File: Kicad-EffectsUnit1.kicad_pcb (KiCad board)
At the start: 2 copper layers, 100 x 100 mm, 0 parts

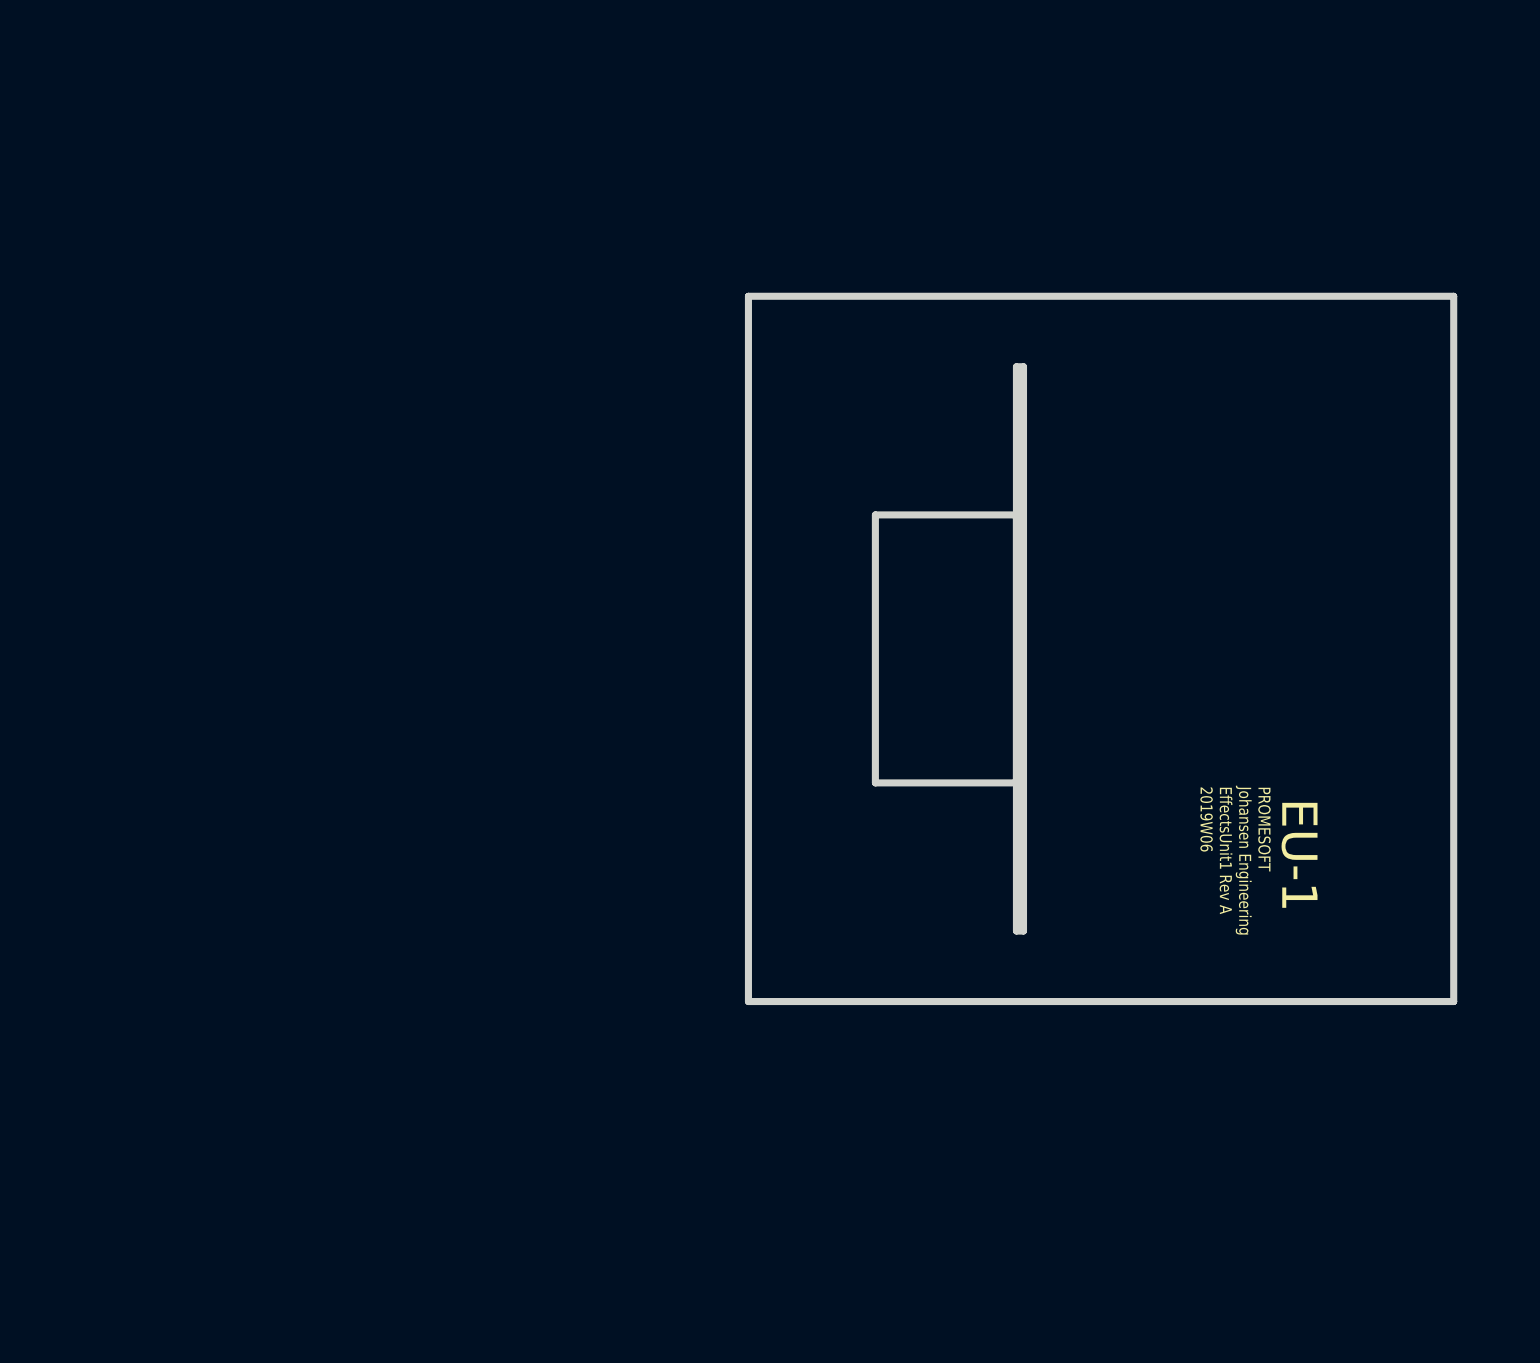
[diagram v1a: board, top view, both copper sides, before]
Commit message: anti latchup initiated
inspiration:
https://www.electrosmash.com/images/tech/pt2399/PT2399_Transistor_Current_Sink_Pin6.png
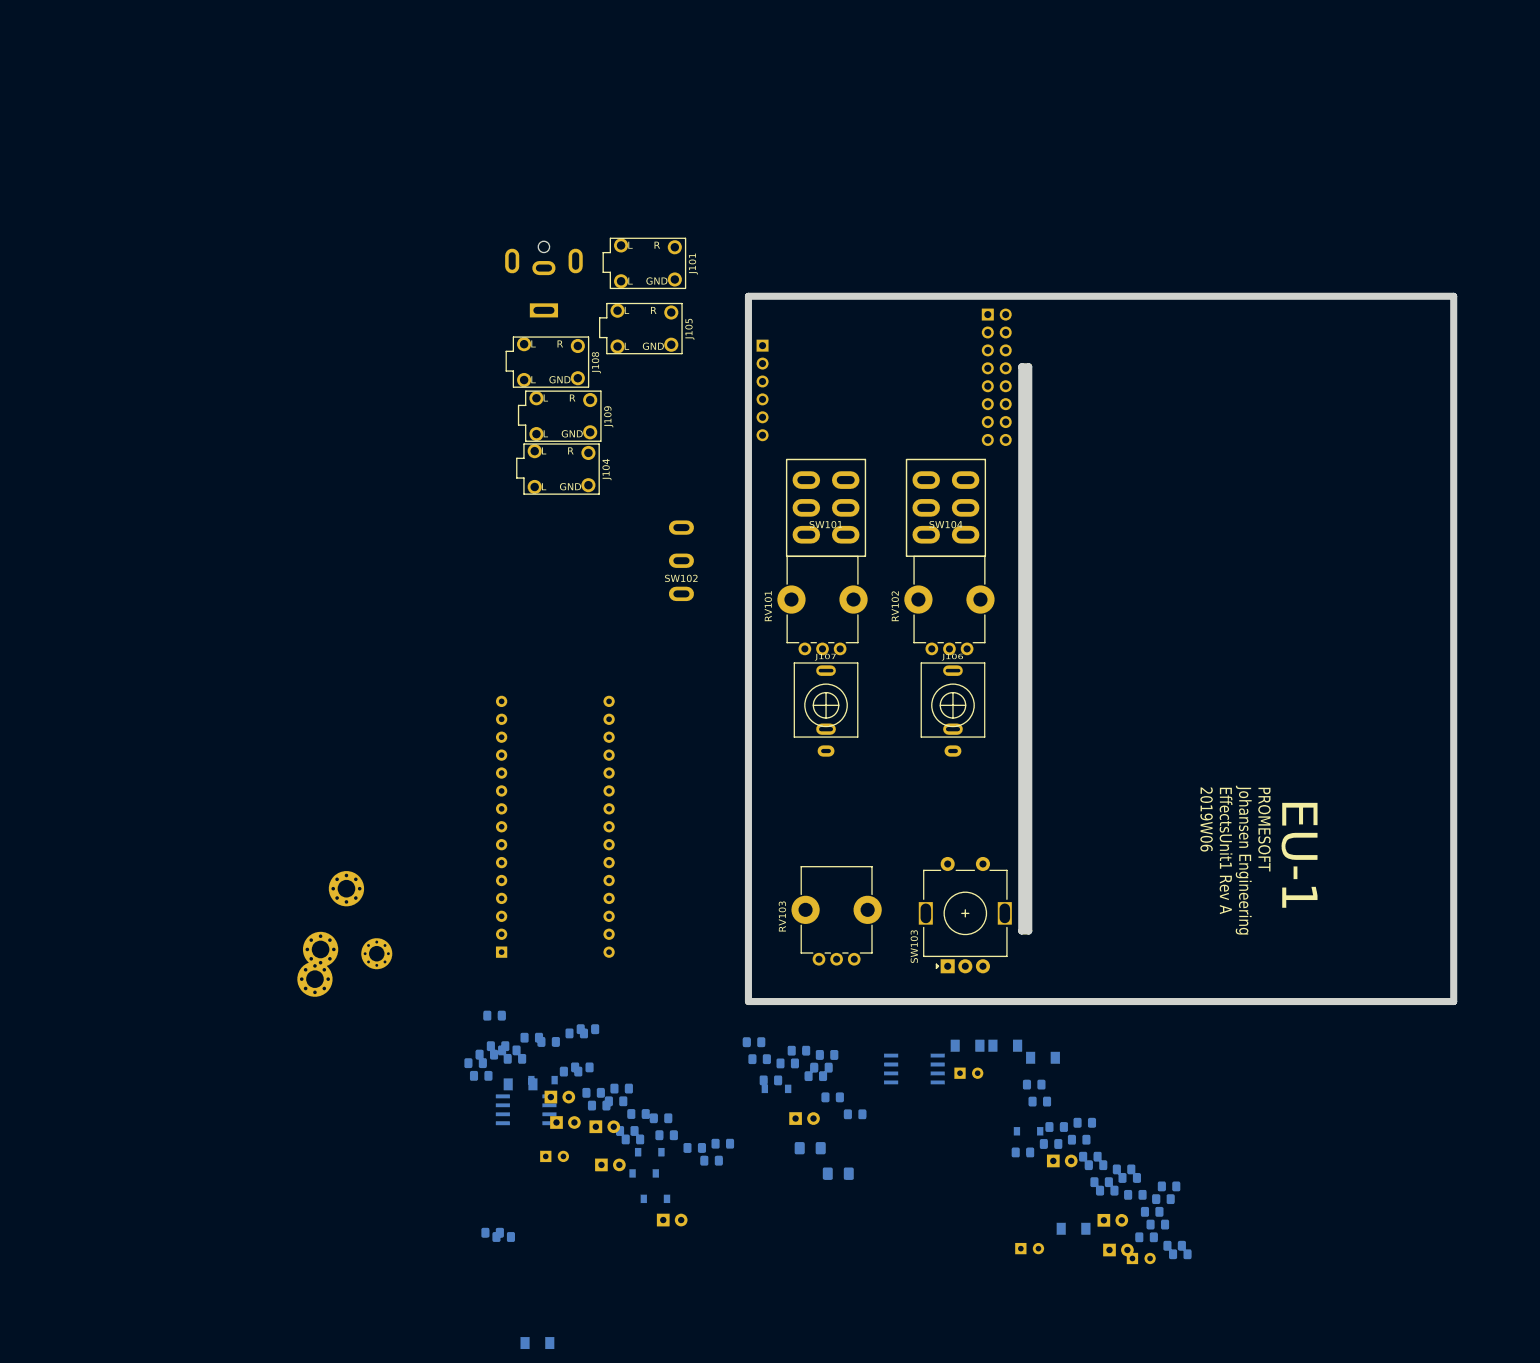
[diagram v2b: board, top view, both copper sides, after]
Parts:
- added A101: Arduino_Nano_v3.x, Module:Arduino_Nano, B.Cu at (65.0, 143.0)
- added C101: 100uF, Capacitor_THT:CP_Radial_D5.0mm_P2.50mm, B.Cu at (138.6, 185.0)
- added C102: 100n, Capacitor_SMD:C_0805_2012Metric_Pad1.15x1.40mm_HandSolder, B.Cu at (161.2, 185.8)
- added C103: 100n, Capacitor_SMD:C_0805_2012Metric_Pad1.15x1.40mm_HandSolder, B.Cu at (66.1, 156.9)
- added C104: 100n, Capacitor_SMD:C_0805_2012Metric_Pad1.15x1.40mm_HandSolder, B.Cu at (64.0, 152.0)
- added C105: 100uF, Capacitor_THT:CP_Radial_D5.0mm_P2.50mm, B.Cu at (130.0, 160.2)
- added C106: 100uF 16v, Capacitor_THT:CP_Radial_D5.0mm_P2.50mm, B.Cu at (71.3, 172.0)
- added C107: 100n, Capacitor_SMD:C_0805_2012Metric_Pad1.15x1.40mm_HandSolder, B.Cu at (64.5, 156.3)
- added C108: 100n, Capacitor_SMD:C_0805_2012Metric_Pad1.15x1.40mm_HandSolder, B.Cu at (62.9, 157.5)
- added C109: 100n, Capacitor_SMD:C_0805_2012Metric_Pad1.15x1.40mm_HandSolder, B.Cu at (65.3, 183.4)
- added C110: 100uF 16v, Capacitor_THT:CP_Radial_D5.0mm_P2.50mm, B.Cu at (154.4, 186.4)
- added C111: 100n, Capacitor_SMD:C_0805_2012Metric_Pad1.15x1.40mm_HandSolder, B.Cu at (62.1, 160.5)
- added C112: 100n, Capacitor_SMD:C_0805_2012Metric_Pad1.15x1.40mm_HandSolder, B.Cu at (61.3, 158.7)
- added C113: 100n, Capacitor_SMD:C_0805_2012Metric_Pad1.15x1.40mm_HandSolder, B.Cu at (148.5, 172.0)
- added C114: 47n, Capacitor_SMD:C_0805_2012Metric_Pad1.15x1.40mm_HandSolder, B.Cu at (138.9, 171.4)
- added C115: 100n, Capacitor_SMD:C_0805_2012Metric_Pad1.15x1.40mm_HandSolder, B.Cu at (69.3, 155.1)
- added C116: 100n, Capacitor_SMD:C_0805_2012Metric_Pad1.15x1.40mm_HandSolder, B.Cu at (150.9, 176.8)
- added C117: 33n, Capacitor_SMD:C_0805_2012Metric_Pad1.15x1.40mm_HandSolder, B.Cu at (160.4, 184.6)
- added C118: 100n, Capacitor_SMD:C_0805_2012Metric_Pad1.15x1.40mm_HandSolder, B.Cu at (94.8, 172.6)
- added C119: 33n, Capacitor_SMD:C_0805_2012Metric_Pad1.15x1.40mm_HandSolder, B.Cu at (154.1, 175.0)
- added C120: 44n, Capacitor_SMD:C_0805_2012Metric_Pad1.15x1.40mm_HandSolder, B.Cu at (107.2, 157.0)
- added C121: 44n, Capacitor_SMD:C_0805_2012Metric_Pad1.15x1.40mm_HandSolder, B.Cu at (84.4, 166.0)
- added D101: 1N1007, Diode_SMD:D_SOD-123, B.Cu at (70.9, 161.1)
- added D102: 1N1007, Diode_SMD:D_SOD-123, B.Cu at (85.2, 174.4)
- added D103: LED1, LED_THT:LED_D3.0mm, B.Cu at (72.8, 167.2)
- added D104: LED2, LED_THT:LED_D3.0mm, B.Cu at (79.2, 173.2)
- added D105: LED3, LED_THT:LED_D3.0mm, B.Cu at (151.2, 185.2)
- added D106: 1N1007, Diode_SMD:D_SOD-123, B.Cu at (139.7, 168.4)
- added D107: LED4, LED_THT:LED_D3.0mm, B.Cu at (87.9, 181.0)
- added D108: 1N1007, Diode_SMD:D_SOD-123, B.Cu at (86.8, 178.0)
- added D109: LED_Out10, LED_THT:LED_D3.0mm, B.Cu at (72.0, 163.5)
- added D110: 1N1007, Diode_SMD:D_SOD-123, B.Cu at (86.0, 171.4)
- added D111: 1N1007, Diode_SMD:D_SOD-123, B.Cu at (104.0, 162.4)
- added D112: LED_Out11, LED_THT:LED_D3.0mm, B.Cu at (78.4, 167.8)
- added D113: LED_Out12, LED_THT:LED_D3.0mm, B.Cu at (143.2, 172.6)
- added D114: LED_Out13, LED_THT:LED_D3.0mm, B.Cu at (150.4, 181.0)
- added D115: LL4148, Diode_SMD:D_MiniMELF, B.Cu at (146.1, 182.2)
- added D116: LL4148, Diode_SMD:D_MiniMELF, B.Cu at (67.7, 161.7)
- added D117: LED_Out11, LED_SMD:LED_0805_2012Metric_Pad1.15x1.40mm_HandSolder, B.Cu at (63.7, 182.8)
- added D118: LED_CV2, LED_THT:LED_D3.0mm, B.Cu at (106.7, 166.6)
- added D119: LL4148, Diode_SMD:D_MiniMELF, B.Cu at (141.8, 158.0)
- added D120: LL4148, Diode_SMD:D_MiniMELF, B.Cu at (136.4, 156.3)
- added D121: LL4148, Diode_SMD:D_MiniMELF, B.Cu at (131.1, 156.3)
- added D122: LL4148, Diode_SMD:D_MiniMELF, B.Cu at (70.1, 198.4)
- added F101: Polyfuse, Fuse:Fuse_1206_3216Metric_Pad1.42x1.75mm_HandSolder, B.Cu at (108.8, 170.8)
- added F102: Polyfuse, Fuse:Fuse_1206_3216Metric_Pad1.42x1.75mm_HandSolder, B.Cu at (112.7, 174.4)
- added H101: 2,5mm, MountingHole:MountingHole_2.5mm_Pad_Via, B.Cu at (39.3, 142.6)
- added H102: 2,5mm, MountingHole:MountingHole_2.5mm_Pad_Via, B.Cu at (38.5, 146.8)
- added H103: 2,2mm, MountingHole:MountingHole_2.5mm_Pad_Via, B.Cu at (43.0, 134.0)
- added H104: 2,2mm, MountingHole:MountingHole_2.2mm_M2_Pad_Via, B.Cu at (47.3, 143.2)
- added J101: In7, Connector_Audio:AudioJack3StereoNarrow-PJ-321, F.Cu at (85.8, 45.3)
- added J102: Doepfer connector, Connector_PinSocket_2.54mm:PinSocket_2x08_P2.54mm_Vertical, B.Cu at (133.9, 52.6)
- added J103: Vin 7-12v, Connector_BarrelJack:BarrelJack_CUI_PJ-063AH_Horizontal, B.Cu at (71.0, 52.0)
- added J104: In6, Connector_Audio:AudioJack3StereoNarrow-PJ-321, F.Cu at (73.5, 74.5)
- added J105: In3, Connector_Audio:AudioJack3StereoNarrow-PJ-321, F.Cu at (85.2, 54.6)
- added J106: Out10, AJ-Dropbox-Kicad:PJ301SM, F.Cu at (129.0, 108.0)
- added J107: Out11, AJ-Dropbox-Kicad:PJ301SM, F.Cu at (111.0, 108.0)
- added J108: Out12, Connector_Audio:AudioJack3StereoNarrow-PJ-321, F.Cu at (72.0, 59.3)
- added J109: Out13, Connector_Audio:AudioJack3StereoNarrow-PJ-321, F.Cu at (73.8, 67.0)
- added J110: Power Conn, Connector_PinHeader_2.54mm:PinHeader_1x06_P2.54mm_Vertical, B.Cu at (102.0, 57.0)
- added R101: 10k, Resistor_SMD:R_0805_2012Metric_Pad1.15x1.40mm_HandSolder, B.Cu at (142.9, 170.2)
- added R102: 10M, Resistor_SMD:R_0805_2012Metric_Pad1.15x1.40mm_HandSolder, B.Cu at (158.0, 181.6)
- added R103: 10k, Resistor_SMD:R_0805_2012Metric_Pad1.15x1.40mm_HandSolder, B.Cu at (150.1, 175.6)
- added R104: 10k, Resistor_SMD:R_0805_2012Metric_Pad1.15x1.40mm_HandSolder, B.Cu at (71.7, 155.7)
- added R105: 10k, Resistor_SMD:R_0805_2012Metric_Pad1.15x1.40mm_HandSolder, B.Cu at (83.6, 169.6)
- added R106: 680R, Resistor_SMD:R_0805_2012Metric_Pad1.15x1.40mm_HandSolder, B.Cu at (115.1, 166.0)
- added R107: 10k, Resistor_SMD:R_0805_2012Metric_Pad1.15x1.40mm_HandSolder, B.Cu at (103.2, 161.2)
- added R108: 10k, Resistor_SMD:R_0805_2012Metric_Pad1.15x1.40mm_HandSolder, B.Cu at (101.6, 158.2)
- added R109: 680R, Resistor_SMD:R_0805_2012Metric_Pad1.15x1.40mm_HandSolder, B.Cu at (141.3, 164.2)
- added R110: 680R, Resistor_SMD:R_0805_2012Metric_Pad1.15x1.40mm_HandSolder, B.Cu at (111.9, 163.6)
- added R111: 11k, Resistor_SMD:R_0805_2012Metric_Pad1.15x1.40mm_HandSolder, B.Cu at (100.8, 155.8)
- added R112: 11k, Resistor_SMD:R_0805_2012Metric_Pad1.15x1.40mm_HandSolder, B.Cu at (156.5, 183.4)
- added R113: 680R, Resistor_SMD:R_0805_2012Metric_Pad1.15x1.40mm_HandSolder, B.Cu at (78.0, 162.9)
- added R114: 680R, Resistor_SMD:R_0805_2012Metric_Pad1.15x1.40mm_HandSolder, B.Cu at (82.8, 168.4)
- added R115: 110R, Resistor_SMD:R_0805_2012Metric_Pad1.15x1.40mm_HandSolder, B.Cu at (149.3, 173.2)
- added R116: 680R, Resistor_SMD:R_0805_2012Metric_Pad1.15x1.40mm_HandSolder, B.Cu at (157.2, 179.8)
- added R117: 11k, Resistor_SMD:R_0805_2012Metric_Pad1.15x1.40mm_HandSolder, B.Cu at (154.9, 177.4)
- added R118: 680R, Resistor_SMD:R_0805_2012Metric_Pad1.15x1.40mm_HandSolder, B.Cu at (143.7, 167.8)
- added R119: 22k, Resistor_SMD:R_0805_2012Metric_Pad1.15x1.40mm_HandSolder, B.Cu at (92.4, 170.8)
- added R120: 22k, Resistor_SMD:R_0805_2012Metric_Pad1.15x1.40mm_HandSolder, B.Cu at (105.6, 158.8)
- added R121: 680R, Resistor_SMD:R_0805_2012Metric_Pad1.15x1.40mm_HandSolder, B.Cu at (109.6, 160.6)
- added R122: 220R, Resistor_SMD:R_0805_2012Metric_Pad1.15x1.40mm_HandSolder, B.Cu at (74.9, 159.9)
- added R123: 220R, Resistor_SMD:R_0805_2012Metric_Pad1.15x1.40mm_HandSolder, B.Cu at (78.8, 164.7)
- added R124: 220k, Resistor_SMD:R_0805_2012Metric_Pad1.15x1.40mm_HandSolder, B.Cu at (66.9, 158.1)
- added R125: 10k, Resistor_SMD:R_0805_2012Metric_Pad1.15x1.40mm_HandSolder, B.Cu at (76.4, 159.3)
- added R126: 10k, Resistor_SMD:R_0805_2012Metric_Pad1.15x1.40mm_HandSolder, B.Cu at (88.4, 169.0)
- added R127: 10k, Resistor_SMD:R_0805_2012Metric_Pad1.15x1.40mm_HandSolder, B.Cu at (81.2, 164.1)
- added R128: 3k3, Resistor_SMD:R_0805_2012Metric_Pad1.15x1.40mm_HandSolder, B.Cu at (87.6, 166.6)
- added R129: 33k, Resistor_SMD:R_0805_2012Metric_Pad1.15x1.40mm_HandSolder, B.Cu at (146.9, 169.6)
- added R130: 133R, Resistor_SMD:R_0805_2012Metric_Pad1.15x1.40mm_HandSolder, B.Cu at (75.7, 154.5)
- added R131: 33k, Resistor_SMD:R_0805_2012Metric_Pad1.15x1.40mm_HandSolder, B.Cu at (153.3, 173.8)
- added R132: 33k, Resistor_SMD:R_0805_2012Metric_Pad1.15x1.40mm_HandSolder, B.Cu at (110.3, 159.4)
- added R133: 330k, Resistor_SMD:R_0805_2012Metric_Pad1.15x1.40mm_HandSolder, B.Cu at (158.8, 178.0)
- added R134: 33k, Resistor_SMD:R_0805_2012Metric_Pad1.15x1.40mm_HandSolder, B.Cu at (82.0, 162.3)
- added R135: 44k, Resistor_SMD:R_0805_2012Metric_Pad1.15x1.40mm_HandSolder, B.Cu at (140.5, 161.8)
- added R136: 44k, Resistor_SMD:R_0805_2012Metric_Pad1.15x1.40mm_HandSolder, B.Cu at (147.7, 167.2)
- added R137: 144R, Resistor_SMD:R_0805_2012Metric_Pad1.15x1.40mm_HandSolder, B.Cu at (77.2, 153.9)
- added R138: 44k, Resistor_SMD:R_0805_2012Metric_Pad1.15x1.40mm_HandSolder, B.Cu at (159.6, 176.2)
- added R139: 44k, Resistor_SMD:R_0805_2012Metric_Pad1.15x1.40mm_HandSolder, B.Cu at (111.1, 157.6)
- added R140: 440k, Resistor_SMD:R_0805_2012Metric_Pad1.15x1.40mm_HandSolder, B.Cu at (96.4, 170.2)
- added RV101: 10k, Potentiometer_THT:Potentiometer_Alps_RK09K_Single_Vertical, F.Cu at (113.0, 100.0)
- added RV102: 10k, Potentiometer_THT:Potentiometer_Alps_RK09K_Single_Vertical, F.Cu at (131.0, 100.0)
- added RV103: 100k, Potentiometer_THT:Potentiometer_Alps_RK09K_Single_Vertical, F.Cu at (115.0, 144.0)
- added SW101: SW_DPDT_x2, AJ-Dropbox-Kicad:SPDTx2, F.Cu at (111.0, 80.0)
- added SW102: SW_SPDT, AJ-Dropbox-Kicad:SP1MS1, F.Cu at (90.5, 87.5)
- added SW103: Rotary_Encoder_Switch, Rotary_Encoder:RotaryEncoder_Alps_EC11E-Switch_Vertical_H20mm, F.Cu at (128.2, 145.0)
- added SW104: SW_DPDT_x2, AJ-Dropbox-Kicad:SPDTx2, F.Cu at (128.0, 80.0)
- added U101: TL072, AJ-Dropbox-Kicad:AJ_SO-8_5.3x6.2mm_P1.27mm, B.Cu at (123.5, 159.6)
- added U102: TL072, AJ-Dropbox-Kicad:AJ_SO-8_5.3x6.2mm_P1.27mm, B.Cu at (68.5, 165.3)
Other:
- outline, holes or cut-outs redrawn

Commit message: Footprints
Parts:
- added C201: 100uF 16v, Capacitor_THT:CP_Radial_D5.0mm_P2.50mm, F.Cu at (154.6, 35.7)
- added C202: 100n, Capacitor_SMD:C_0805_2012Metric_Pad1.15x1.40mm_HandSolder, F.Cu at (204.3, 24.4)
- added C203: 100n, Capacitor_SMD:C_0805_2012Metric_Pad1.15x1.40mm_HandSolder, F.Cu at (204.3, 26.3)
- added C204: 100n, Capacitor_SMD:C_0805_2012Metric_Pad1.15x1.40mm_HandSolder, F.Cu at (193.1, 26.3)
- added C205: 100uF 16v, Capacitor_THT:CP_Radial_D5.0mm_P2.50mm, F.Cu at (173.1, 41.5)
- added C206: 100uF 16v, Capacitor_THT:CP_Radial_D5.0mm_P2.50mm, F.Cu at (167.5, 41.5)
- added C207: 100n, Capacitor_SMD:C_0805_2012Metric_Pad1.15x1.40mm_HandSolder, F.Cu at (195.8, 36.1)
- added C208: 100n, Capacitor_SMD:C_0805_2012Metric_Pad1.15x1.40mm_HandSolder, F.Cu at (188.3, 31.0)
- added C209: 100n, Capacitor_SMD:C_0805_2012Metric_Pad1.15x1.40mm_HandSolder, F.Cu at (204.2, 18.5)
- added C210: 100uF 16v, Capacitor_THT:CP_Radial_D5.0mm_P2.50mm, F.Cu at (204.0, 14.8)
- added C211: 3n3, Capacitor_SMD:C_0805_2012Metric_Pad1.15x1.40mm_HandSolder, F.Cu at (160.5, 33.9)
- added C212: 4u7, Capacitor_SMD:C_0805_2012Metric_Pad1.15x1.40mm_HandSolder, F.Cu at (160.5, 35.8)
- added C213: 4u7, Capacitor_SMD:C_0805_2012Metric_Pad1.15x1.40mm_HandSolder, F.Cu at (200.2, 19.7)
- added C214: 560p, Capacitor_SMD:C_0805_2012Metric_Pad1.15x1.40mm_HandSolder, F.Cu at (200.2, 21.7)
- added C215: 100uF 16v, Capacitor_THT:CP_Radial_D5.0mm_P2.50mm, F.Cu at (194.3, 21.5)
- added C216: 10u, Capacitor_SMD:C_0805_2012Metric_Pad1.15x1.40mm_HandSolder, F.Cu at (188.3, 33.0)
- added C217: 10u, Capacitor_SMD:C_0805_2012Metric_Pad1.15x1.40mm_HandSolder, F.Cu at (193.1, 28.3)
- added C218: 10n, Capacitor_SMD:C_0805_2012Metric_Pad1.15x1.40mm_HandSolder, F.Cu at (193.1, 30.2)
- added C219: 560p, Capacitor_SMD:C_0805_2012Metric_Pad1.15x1.40mm_HandSolder, F.Cu at (188.3, 34.9)
- added C220: 82n, Capacitor_SMD:C_0805_2012Metric_Pad1.15x1.40mm_HandSolder, F.Cu at (200.2, 23.6)
- added C221: 3n3, Capacitor_SMD:C_0805_2012Metric_Pad1.15x1.40mm_HandSolder, F.Cu at (196.8, 25.6)
- added C222: 1u, Capacitor_SMD:C_0805_2012Metric_Pad1.15x1.40mm_HandSolder, F.Cu at (184.5, 40.1)
- added C223: 100n, Capacitor_SMD:C_0805_2012Metric_Pad1.15x1.40mm_HandSolder, F.Cu at (196.8, 27.5)
- added C224: 82n, Capacitor_SMD:C_0805_2012Metric_Pad1.15x1.40mm_HandSolder, F.Cu at (203.9, 20.5)
- added C225: 100n, Capacitor_SMD:C_0805_2012Metric_Pad1.15x1.40mm_HandSolder, F.Cu at (208.0, 18.5)
- added C226: 100n, Capacitor_SMD:C_0805_2012Metric_Pad1.15x1.40mm_HandSolder, F.Cu at (203.9, 22.4)
- added D201: 1N1007, Diode_SMD:D_SOD-123, F.Cu at (188.8, 28.9)
- added D202: 1N1007, Diode_SMD:D_SOD-123, F.Cu at (155.4, 43.1)
- added D203: 1N1007, Diode_SMD:D_SOD-123, F.Cu at (188.8, 26.5)
- added D204: 5v6, Diode_SMD:D_MELF-RM10_Universal_Handsoldering, F.Cu at (159.4, 40.3)
- added D205: 1N1007, Diode_SMD:D_SOD-123, F.Cu at (160.1, 43.1)
- added J201: In, AJ-Dropbox-Kicad:PJ301SM, F.Cu at (188.1, 18.1)
- added J202: Out, AJ-Dropbox-Kicad:PJ301SM, F.Cu at (181.9, 31.9)
- added P201: HEADER_2x5_Doepfer, Connector_PinHeader_2.54mm:PinHeader_2x05_P2.54mm_Vertical, F.Cu at (179.1, 13.8)
- added Q201: BC337, Package_TO_SOT_THT:TO-92_Inline, F.Cu at (178.6, 41.9)
- added Q202: PZT2222A, Package_TO_SOT_SMD:SOT-23, F.Cu at (204.2, 29.1)
- added Q203: PZT2222A, Package_TO_SOT_SMD:SOT-23, F.Cu at (199.4, 32.2)
- added R201: 10k, Resistor_SMD:R_0805_2012Metric_Pad1.15x1.40mm_HandSolder, F.Cu at (200.6, 25.6)
- added R202: 0R, Resistor_SMD:R_0805_2012Metric_Pad1.15x1.40mm_HandSolder, F.Cu at (188.3, 36.9)
- added R203: 15k, Resistor_SMD:R_0805_2012Metric_Pad1.15x1.40mm_HandSolder, F.Cu at (192.1, 32.2)
- added R204: 0R, Resistor_SMD:R_0805_2012Metric_Pad1.15x1.40mm_HandSolder, F.Cu at (192.1, 34.1)
- added R205: 10k, Resistor_SMD:R_0805_2012Metric_Pad1.15x1.40mm_HandSolder, F.Cu at (184.5, 42.1)
- added R206: 10k, Resistor_SMD:R_0805_2012Metric_Pad1.15x1.40mm_HandSolder, F.Cu at (188.3, 38.8)
- added R207: 10k, Resistor_SMD:R_0805_2012Metric_Pad1.15x1.40mm_HandSolder, F.Cu at (188.2, 40.8)
- added R208: 4k7, Resistor_SMD:R_0805_2012Metric_Pad1.15x1.40mm_HandSolder, F.Cu at (192.1, 36.1)
- added R209: 5k6, Resistor_SMD:R_0805_2012Metric_Pad1.15x1.40mm_HandSolder, F.Cu at (195.8, 32.2)
- added R210: 15k, Resistor_SMD:R_0805_2012Metric_Pad1.15x1.40mm_HandSolder, F.Cu at (200.6, 27.5)
- added R211: 10k, Resistor_SMD:R_0805_2012Metric_Pad1.15x1.40mm_HandSolder, F.Cu at (196.8, 29.5)
- added R212: 10k, Resistor_SMD:R_0805_2012Metric_Pad1.15x1.40mm_HandSolder, F.Cu at (207.7, 20.5)
- added R213: 100k, Resistor_SMD:R_0805_2012Metric_Pad1.15x1.40mm_HandSolder, F.Cu at (207.7, 22.4)
- added R214: 120k, Resistor_SMD:R_0805_2012Metric_Pad1.15x1.40mm_HandSolder, F.Cu at (200.6, 29.5)
- added R215: 22k, Resistor_SMD:R_0805_2012Metric_Pad1.15x1.40mm_HandSolder, F.Cu at (195.8, 34.1)
- added R216: 150R, Resistor_SMD:R_0805_2012Metric_Pad1.15x1.40mm_HandSolder, F.Cu at (192.1, 38.0)
- added RV201: 50k, Potentiometer_THT:Potentiometer_China_RK09_Single_Vertical_AJ, F.Cu at (164.0, 34.5)
- added RV202: 20k, Potentiometer_THT:Potentiometer_Alps_RK09K_Single_Vertical, F.Cu at (164.0, 21.2)
- added U201: TL072, AJ-Dropbox-Kicad:AJ_SO-8_5.3x6.2mm_P1.27mm, F.Cu at (197.5, 15.4)
- added U202: PT2399, Package_DIP:DIP-16_W7.62mm, F.Cu at (154.1, 13.6)
- J101, J104, J105, J108, J109: footprint Connector_Audio:AudioJack3StereoNarrow-PJ-321 -> AJ-Dropbox-Kicad:PJ301SM
- J103: footprint Connector_BarrelJack:BarrelJack_CUI_PJ-063AH_Horizontal -> Connector_BarrelJack:BarrelJack_Horizontal
- RV101: value 10k -> 10k_O10; footprint Potentiometer_THT:Potentiometer_Alps_RK09K_Single_Vertical -> Potentiometer_THT:Potentiometer_China_RK09_Single_Vertical_AJ
- RV102: value 10k -> 10k_O11; footprint Potentiometer_THT:Potentiometer_Alps_RK09K_Single_Vertical -> Potentiometer_THT:Potentiometer_China_RK09_Single_Vertical_AJ
- RV103: value 100k -> 100k_O12; footprint Potentiometer_THT:Potentiometer_Alps_RK09K_Single_Vertical -> Potentiometer_THT:Potentiometer_China_RK09_Single_Vertical_AJ
- SW101: value SW_DPDT_x2 -> Dist 10
- SW102: value SW_SPDT -> Crush A3
- SW104: value SW_DPDT_x2 -> Dist 12
- moved D108 125.3 mm to (26.8, 68.0)
- moved D112 125.3 mm to (18.4, 57.8)
- moved D117 125.3 mm to (3.72, 72.8)
- moved R128 125.3 mm to (27.6, 56.6)
- moved U102 125.3 mm to (8.48, 55.3)
- moved C103 125.3 mm to (6.09, 46.9)
- moved C106 125.3 mm to (11.3, 62.0)
- moved C108 125.3 mm to (2.90, 47.5)
- moved C109 125.3 mm to (5.29, 73.4)
- moved C111 125.3 mm to (2.11, 50.5)
- moved C112 125.3 mm to (1.31, 48.7)
- moved C121 125.3 mm to (24.4, 56.0)
- moved D101 125.3 mm to (10.9, 51.1)
- moved D102 125.3 mm to (25.2, 64.4)
- moved D103 125.3 mm to (12.8, 57.2)
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
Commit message: PCB work
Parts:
- added REF**: Gauge_100mm_Grid_Type1_Silk_CopperTop, AJ:Gauge_100mm_Grid_Type1_Silk_CopperTop, F.Cu at (100.0, 150.0)
- moved A101 103.1 mm to (117.0, 54.0), turned to 180 degrees
- moved J102 71.0 mm to (119.0, 126.0)
- moved J110 66.5 mm to (110.0, 126.0)
- moved SW103 26.0 mm to (127.2, 145.0)
- moved RV103 25.0 mm to (112.5, 145.0)
- moved J109 20.0 mm to (87.0, 82.0)
- moved SW102 2.00 mm to (110.0, 65.0)
- moved SW104 2.00 mm to (110.0, 87.0)
- moved SW101 1.00 mm to (130.0, 87.0)
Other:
- outline, holes or cut-outs redrawn
